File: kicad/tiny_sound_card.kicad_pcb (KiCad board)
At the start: 2 copper layers, 91 x 55 mm, 46 parts, among them CON1 BARREL_JACK, IC1 ATMEGA328P-A, J1 TRS_JACK, M1 DFR0299, P1 EXT_PWR, P10 M3Drill, P2 SPKOUT, P4 EXT_I2C, P4 M3Drill, P5 EXT_SW0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

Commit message: Close #1
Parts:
- added R1: 1k, Resistors_ThroughHole:R_Axial_DIN0207_L6.3mm_D2.5mm_P10.16mm_Horizontal, F.Cu at (96.2, 97.5)
- added R4: 1k, Resistors_ThroughHole:R_Axial_DIN0207_L6.3mm_D2.5mm_P10.16mm_Horizontal, F.Cu at (125.8, 110.4)
- moved C6 2.00 mm to (119.5, 103.0)
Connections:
- IC1 pad 13: /ATMEGA_TX -> /D9
- M1 pad 3: /A0 -> Net-(M1-Pad3)
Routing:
- net /ATMEGA_TX: track 44.5 -> 25.7 mm
- net GND: track 674.7 -> 685.1 mm, vias 190 -> 196
- net /D9: track 0.00 -> 9.16 mm
- net /A0: track 41.2 -> 47.8 mm
- net Net-(M1-Pad3): track 0.00 -> 3.41 mm
- net VCC: track 239.8 -> 238.9 mm

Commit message: ロゴ追加
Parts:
- added G***: LOGO, kicad:logo-silk, B.Cu at (116.2, 85.2)
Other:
- board text added: "v0.1"

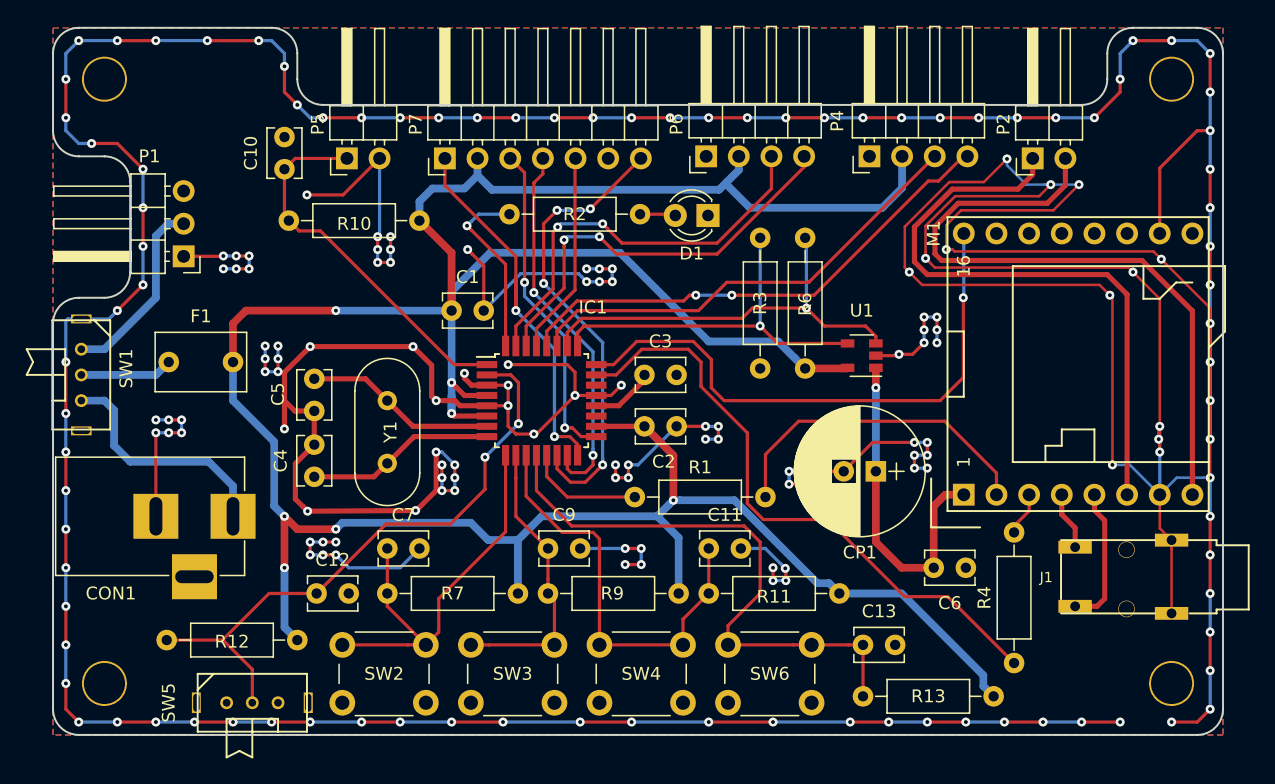
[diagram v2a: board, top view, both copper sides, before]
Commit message: シルクでピンアサイン記述を追加
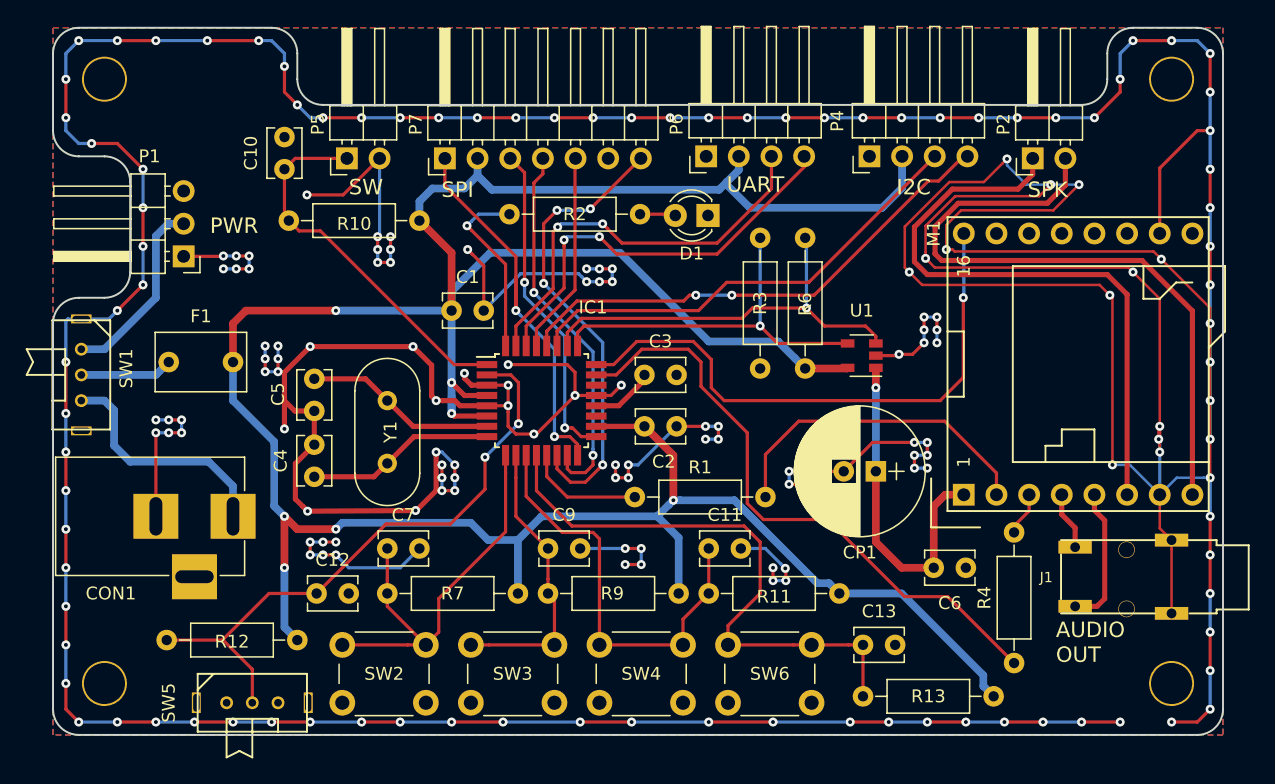
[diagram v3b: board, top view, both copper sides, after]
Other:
- board text added: "A4 SDA"
- board text added: "A5 SCL"
- board text added: "AUDIO OUT"
- board text added: "D0 RXD"
- board text added: "D1 TXD"
- board text added: "D10"
- board text added: "D12 MISO"
- board text added: "D12 MOSI"
- board text added: "D13 SCK"
- board text added: "D3"
- board text added: "D4"
- board text added: "D5"
- board text added: "D6"
- board text added: "D7"
- board text added: "D8"
- board text added: "GND"
- board text added: "I2C"
- board text added: "PWR"
- board text added: "SPI"
- board text added: "SPK"
- board text added: "SPK1"
- board text added: "SPK2"
- board text added: "SW"
- board text added: "UART"
- board text added: "VCC"
- board text added: "~RST"
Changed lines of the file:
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@@
     (area 50.924999 60.924999 142.075001 116.075001)
     (thickness 1.6)
-    (drawings 63)
+    (drawings 97)
     (tracks 883)
     (zones 0)
@@
       (xy -6.711209 5.37225)) (layer B.SilkS) (width 0.01))
   )
+  (gr_text PWR (at 63.2 76.4) (layer F.SilkS)
+    (effects (font (size 1.2 1.2) (thickness 0.2)) (justify left))
+  )
+  (gr_text SW (at 74 73.4) (layer F.SilkS)
+    (effects (font (size 1.2 1.2) (thickness 0.2)) (justify left))
+  )
+  (gr_text SPI (at 81.2 73.6) (layer F.SilkS)
+    (effects (font (size 1.2 1.2) (thickness 0.2)) (justify left))
+  )
+  (gr_text UART (at 103.4 73.2) (layer F.SilkS)
+    (effects (font (size 1.2 1.2) (thickness 0.2)) (justify left))
+  )
+  (gr_text I2C (at 116.6 73.4) (layer F.SilkS)
+    (effects (font (size 1.2 1.2) (thickness 0.2)) (justify left))
+  )
+  (gr_text SPK (at 126.8 73.6) (layer F.SilkS)
+    (effects (font (size 1.2 1.2) (thickness 0.2)) (justify left))
+  )
+  (gr_text "AUDIO\nOUT" (at 129 108.8) (layer F.SilkS)
+    (effects (font (size 1.2 1.2) (thickness 0.2)) (justify left))
+  )
+  (gr_text GND (at 65.4 78.8) (layer B.SilkS)
+    (effects (font (size 0.8 0.8) (thickness 0.15)) (justify left mirror))
+  )
+  (gr_text GND (at 65.2 73.8) (layer B.SilkS)
+    (effects (font (size 0.8 0.8) (thickness 0.15)) (justify left mirror))
+  )
+  (gr_text VCC (at 65.2 76.4) (layer B.SilkS)
+    (effects (font (size 0.8 0.8) (thickness 0.15)) (justify left mirror))
+  )
+  (gr_text D8 (at 107.6 109) (layer B.SilkS)
+    (effects (font (size 0.8 0.8) (thickness 0.15)) (justify left mirror))
+  )
+  (gr_text D7 (at 97.4 109) (layer B.SilkS)
+    (effects (font (size 0.8 0.8) (thickness 0.15)) (justify left mirror))
+  )
+  (gr_text D6 (at 87.6 109) (layer B.SilkS)
+    (effects (font (size 0.8 0.8) (thickness 0.15)) (justify left mirror))
+  )
+  (gr_text D5 (at 77.4 109) (layer B.SilkS)
+    (effects (font (size 0.8 0.8) (thickness 0.15)) (justify left mirror))
+  )
+  (gr_text D4 (at 67.2 110.6) (layer B.SilkS)
+    (effects (font (size 0.8 0.8) (thickness 0.15)) (justify left mirror))
+  )
+  (gr_text SPK1 (at 129.8 72.8 90) (layer B.SilkS)
+    (effects (font (size 0.7 0.7) (thickness 0.15)) (justify left mirror))
+  )
+  (gr_text SPK2 (at 127.2 72.8 90) (layer B.SilkS)
+    (effects (font (size 0.7 0.7) (thickness 0.15)) (justify left mirror))
+  )
+  (gr_text "A5\nSCL" (at 122.2 72.8 90) (layer B.SilkS)
+    (effects (font (size 0.8 0.8) (thickness 0.15)) (justify left mirror))
+  )
+  (gr_text "A4\nSDA" (at 119.6 72.8 90) (layer B.SilkS)
+    (effects (font (size 0.8 0.8) (thickness 0.15)) (justify left mirror))
+  )
+  (gr_text VCC (at 117 72.8 90) (layer B.SilkS)
+    (effects (font (size 0.8 0.8) (thickness 0.15)) (justify left mirror))
+  )
+  (gr_text GND (at 114.4 72.8 90) (layer B.SilkS)
+    (effects (font (size 0.8 0.8) (thickness 0.15)) (justify left mirror))
+  )
+  (gr_text "D0\nRXD" (at 109.4 72.6 90) (layer B.SilkS)
+    (effects (font (size 0.8 0.8) (thickness 0.15)) (justify left mirror))
+  )
+  (gr_text "D1\nTXD" (at 106.8 72.6 90) (layer B.SilkS)
+    (effects (font (size 0.8 0.8) (thickness 0.15)) (justify left mirror))
+  )
+  (gr_text GND (at 103 73.2 360) (layer B.SilkS)
+    (effects (font (size 0.8 0.8) (thickness 0.15)) (justify left mirror))
+  )
+  (gr_text VCC (at 104.4 72.6 90) (layer B.SilkS)
+    (effects (font (size 0.8 0.8) (thickness 0.15)) (justify left mirror))
+  )
+  (gr_text D10 (at 97.8 73.4) (layer B.SilkS)
+    (effects (font (size 0.8 0.8) (thickness 0.15)) (justify left mirror))
+  )
+  (gr_text GND (at 94.2 73 90) (layer B.SilkS)
+    (effects (font (size 0.8 0.8) (thickness 0.15)) (justify left mirror))
+  )
+  (gr_text ~RST (at 91.6 73 90) (layer B.SilkS)
+    (effects (font (size 0.8 0.8) (thickness 0.15)) (justify left mirror))
+  )
+  (gr_text "D12\nMOSI" (at 89.2 73 90) (layer B.SilkS)
+    (effects (font (size 0.8 0.8) (thickness 0.15)) (justify left mirror))
+  )
+  (gr_text "D13\nSCK" (at 87.6 73.4) (layer B.SilkS)
+    (effects (font (size 0.8 0.8) (thickness 0.15)) (justify left mirror))
+  )
+  (gr_text VCC (at 84 73 90) (layer B.SilkS)
+    (effects (font (size 0.8 0.8) (thickness 0.15)) (justify left mirror))
+  )
+  (gr_text "D12\nMISO" (at 81.4 73 90) (layer B.SilkS)
+    (effects (font (size 0.8 0.8) (thickness 0.15)) (justify left mirror))
+  )
+  (gr_text GND (at 76.4 72.8 90) (layer B.SilkS)
+    (effects (font (size 0.8 0.8) (thickness 0.15)) (justify left mirror))
+  )
+  (gr_text D3 (at 73.8 72.8 90) (layer B.SilkS)
+    (effects (font (size 0.8 0.8) (thickness 0.15)) (justify left mirror))
+  )
   (gr_text v0.1 (at 130.5 114) (layer B.SilkS)
